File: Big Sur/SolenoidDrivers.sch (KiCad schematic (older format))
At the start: 35 parts, among them U1 DRV8806, U2 DRV8806, U3 DRV103H, U4 DRV103H

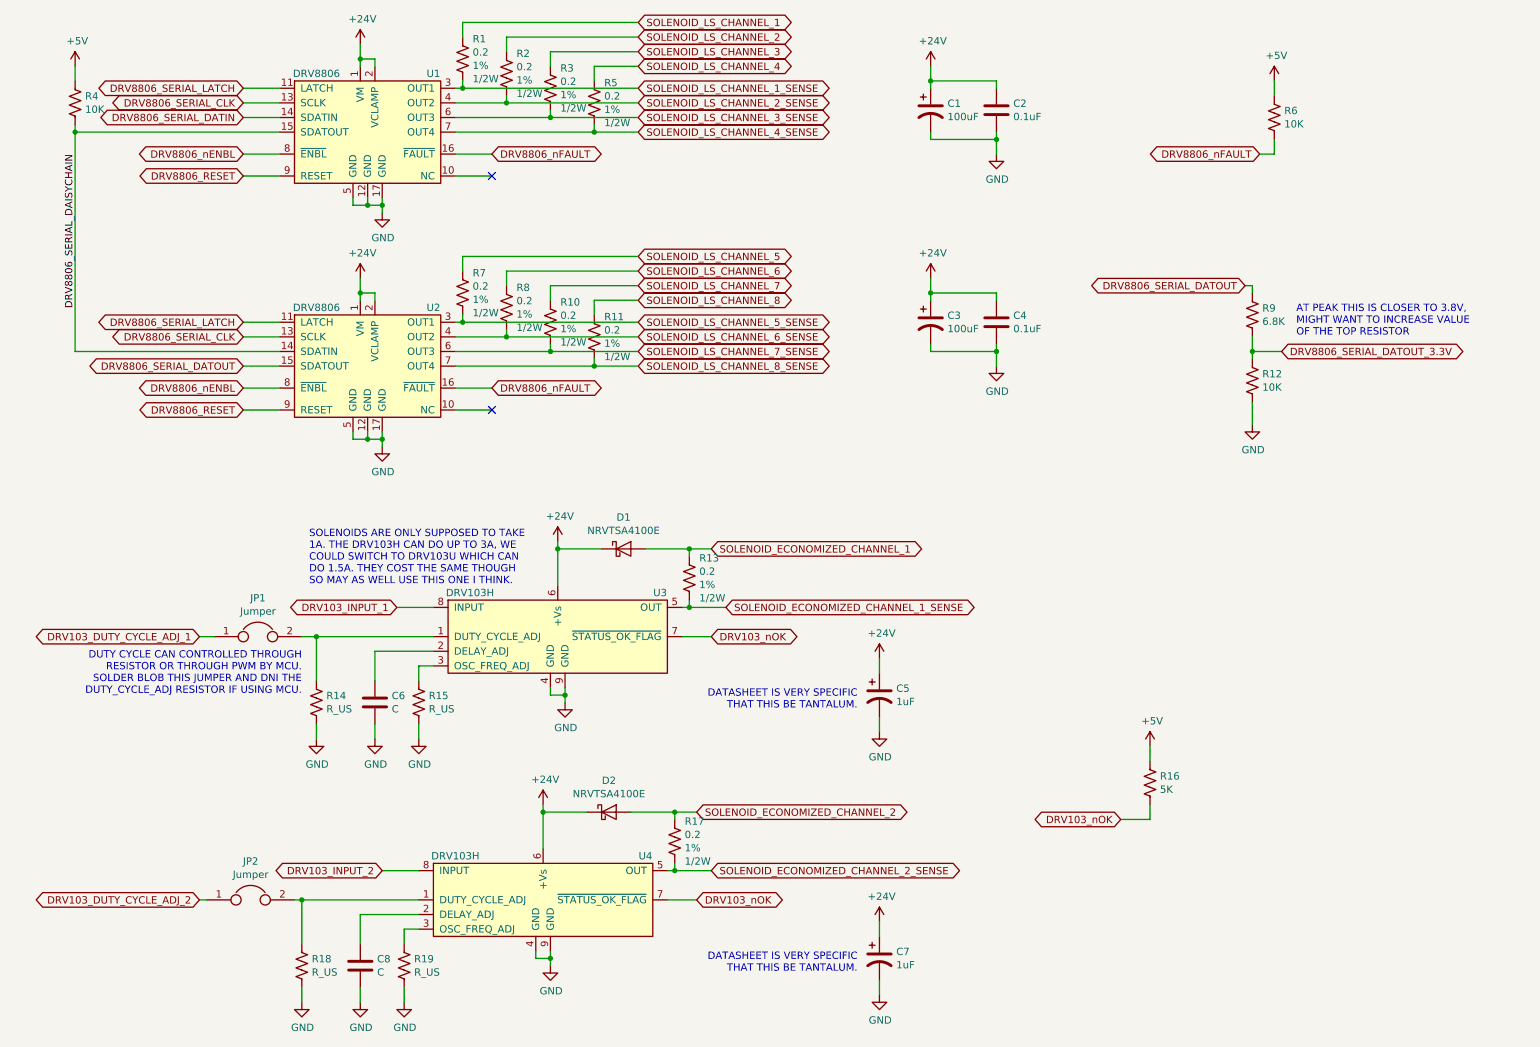
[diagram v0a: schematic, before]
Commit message: Updated current sense, second pump driver, solenoid connectors
-Current sense now uses current sense ICs, connected to Paraduino ADC pins.
-Added second pump driver.
-Connected outputs with XT30 connectors.
-Still need some Paraduino connections, inverter driver, footprints.
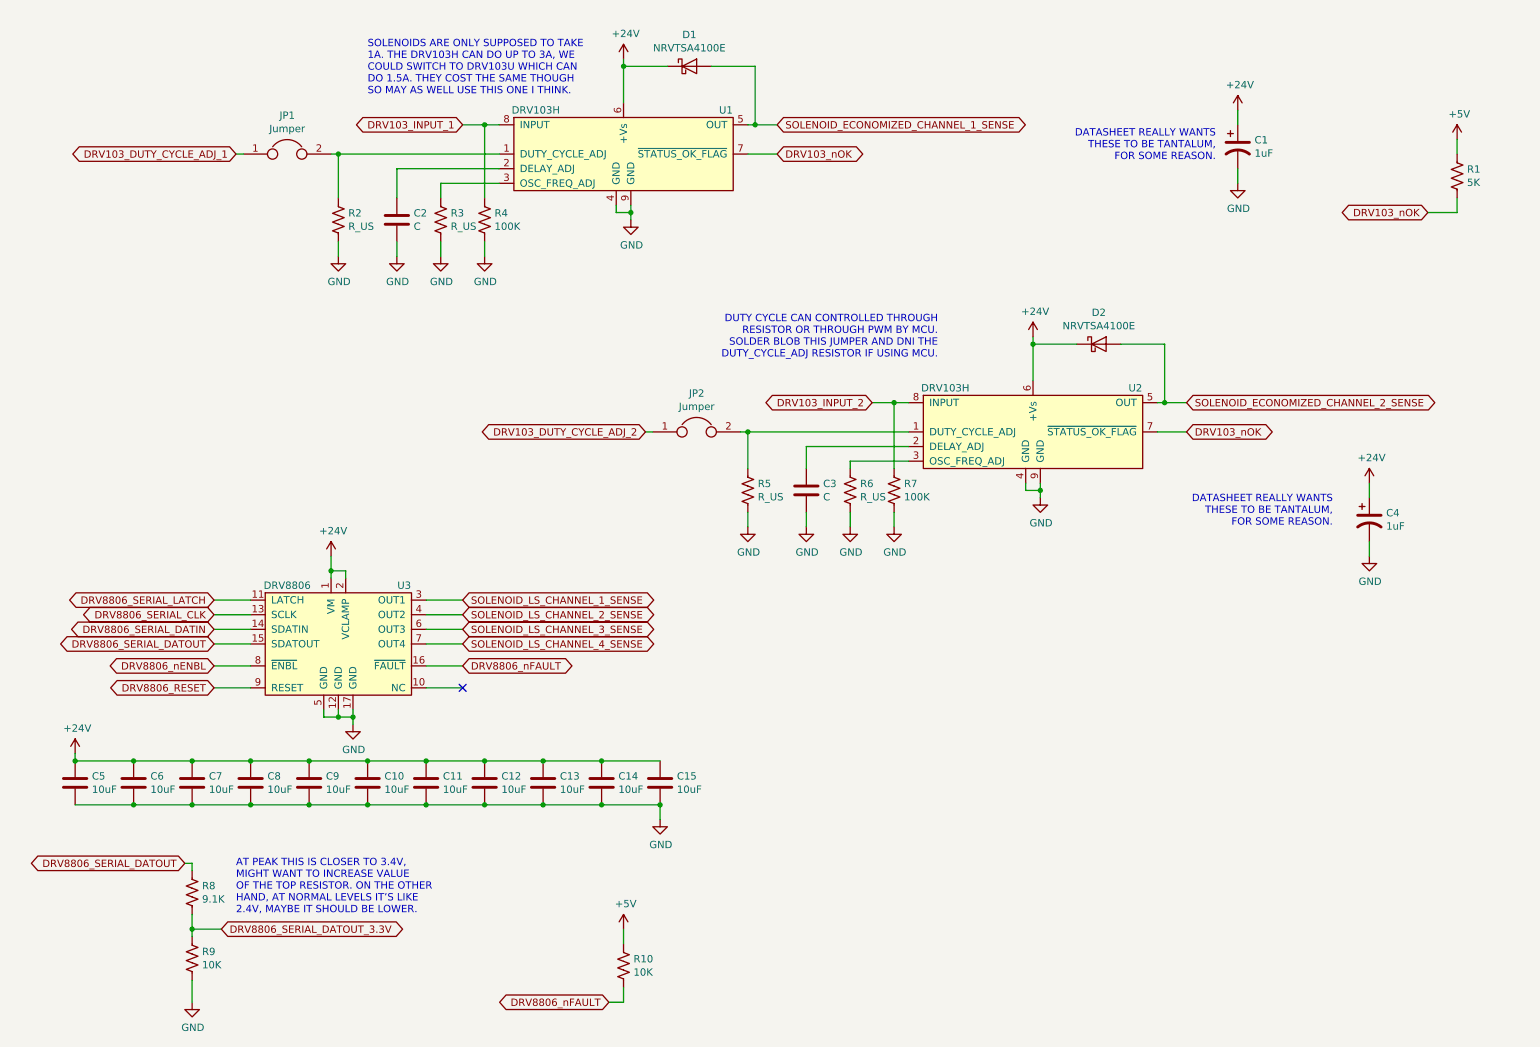
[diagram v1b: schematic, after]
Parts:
- removed C1, C3: 100uF, symbol Device:CP1
- removed C2, C4: 0.1uF, symbol Device:C
- removed C5: 1uF, symbol Device:CP1
- removed R1, R10, R11, R13, R17, R2, R3, R8: 0.2, symbol Device:R_US
- removed R18, R19: R_US, symbol Device:R_US
- removed U2: DRV8806, Package_SO:HTSSOP-16-1EP_4.4x5mm_P0.65mm_EP3.4x5mm_Mask2.46x2.31mm_ThermalVias, symbol BigSurLib:DRV8806
- added C10, C11, C12, C13, C14, C15, C5, C6, C7, C9: 10uF, Capacitor_SMD:C_1210_3225Metric_Pad1.42x2.65mm_HandSolder, symbol Device:C
- added C3: C, symbol Device:C
- added C4: 1uF, symbol Device:CP1
- added R6: R_US, symbol Device:R_US
- C1: renamed from C7; Digikey (none) -> https://www.digikey.ca/product-detail/en/kemet/T491C105K050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; Part Number (none) -> T491C105K050AT
- C8: value C -> 10uF; footprint (none) -> Capacitor_SMD:C_1210_3225Metric_Pad1.42x2.65mm_HandSolder; Digikey (none) -> https://www.digikey.ca/product-detail/en/taiyo-yuden/UMK325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; Part Number (none) -> UMK325BJ106KMHP
- R4: value 10K -> 100K
- R5: value 0.2 -> R_US; Power Rating 1/2W -> (none); Tolerance 1% -> (none)
- R7: value 0.2 -> 100K; Power Rating 1/2W -> (none); Tolerance 1% -> (none)
- R8: renamed from R9; value 6.8K -> 9.1K
- renumbered C6 to C2, R16 to R1, R6 to R10, R14 to R2, R15 to R3, R12 to R9, U3 to U1, U4 to U2, U1 to U3
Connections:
- net SOLENOID_ECONOMIZED_CHANNEL_1 is gone; now on net SOLENOID_ECONOMIZED_CHANNEL_1_SENSE: D1.2 (A)
- net SOLENOID_ECONOMIZED_CHANNEL_2 is gone; now on net SOLENOID_ECONOMIZED_CHANNEL_2_SENSE: D2.2 (A)
- net SOLENOID_LS_CHANNEL_4 is gone; now on net GND: R5.2
- net SOLENOID_LS_CHANNEL_5 is gone; now on net GND: R7.2
- net SOLENOID_LS_CHANNEL_5_SENSE is gone; now on net DRV103_INPUT_2: R7.1
- net +24V: now also C8.1, C10.1, C11.1, C12.1, C13.1, C14.1, C15.1, C4.1, C5.1, C6.1, C7.1, C9.1
- net +5V: no longer R4.1
- net DRV103_INPUT_1: now also R4.1
- net DRV8806_SERIAL_DATOUT: now also U3.15 (SDATOUT)
- net GND: now also R4.2, C10.2, C11.2, C12.2, C13.2, C14.2, C15.2, C3.2, C4.2, C5.2, C6.2, C7.2, C9.2, R6.2
- net SOLENOID_LS_CHANNEL_4_SENSE: no longer R5.1
- net at U2.3 (OSC_FREQ_ADJ): now also R6.1
- net at JP2.2, U2.1 (DUTY_CYCLE_ADJ): now also R5.1
- net at U2.2 (DELAY_ADJ): now also C3.1; no longer C8.1
- removed net DRV8806_SERIAL_DAISYCHAIN: R4.2, U3.15 (SDATOUT)
- no-connect marks 2 -> 1
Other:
- note added: "AT PEAK THIS IS CLOSER TO 3.4V,\nMIGHT WANT TO INCREASE VALUE\nOF THE TOP RESISTOR. ON THE OTHER\nHAND, AT NORMAL LEVELS IT’S LIKE\n2.4V, MAYBE IT SHOULD BE LOWER."
- note added: "DATASHEET REALLY WANTS\nTHESE TO BE TANTALUM,\nFOR SOME REASON."
- note removed: "AT PEAK THIS IS CLOSER TO 3.8V,\nMIGHT WANT TO INCREASE VALUE\nOF THE TOP RESISTOR"
- note removed: "DATASHEET IS VERY SPECIFIC\nTHAT THIS BE TANTALUM."
- moved on the sheet: C1, C2, D1, D2, JP1, R1, R10, R2, R3, R8, R9, U1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

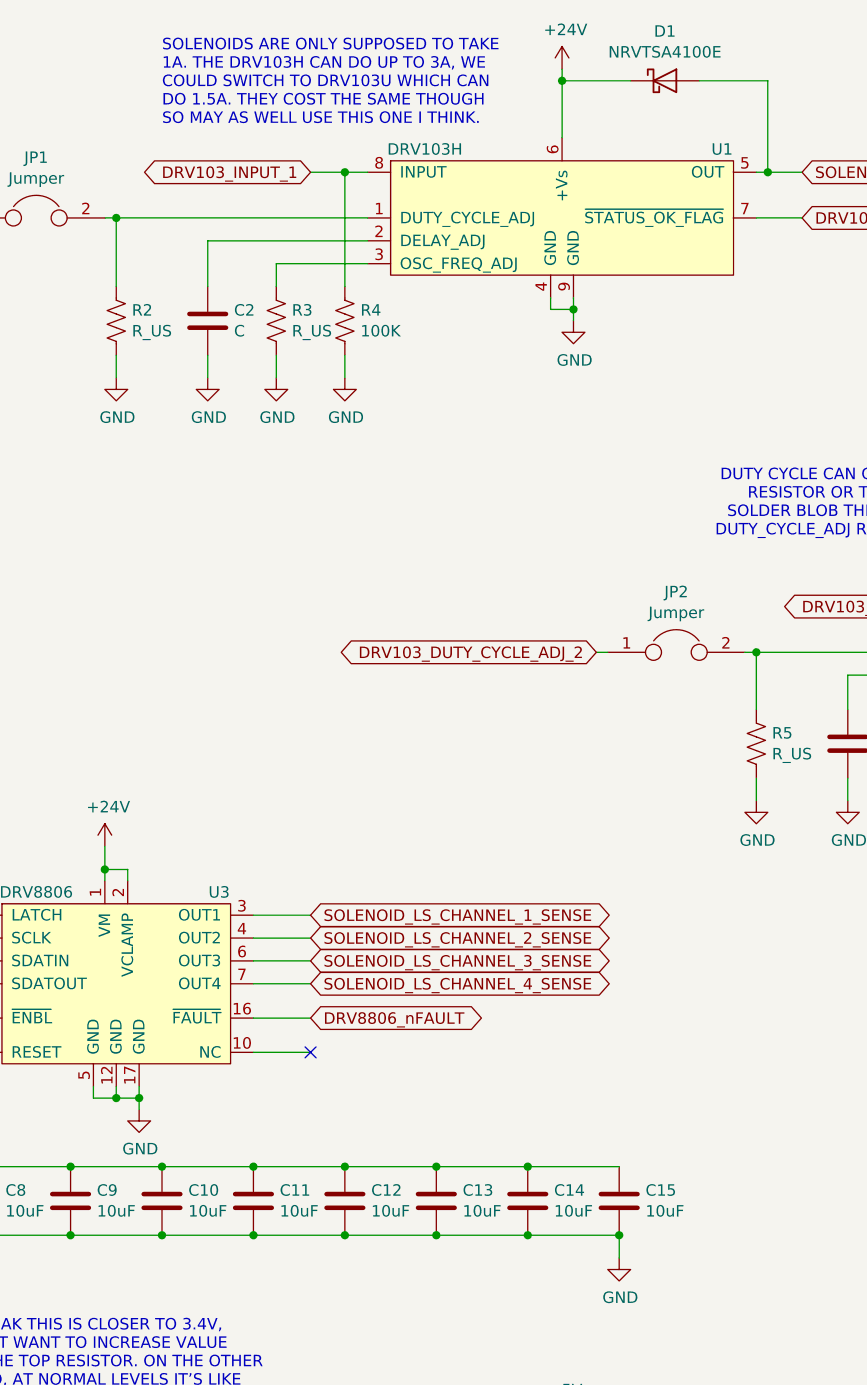
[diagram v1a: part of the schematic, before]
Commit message: Removed Inverter
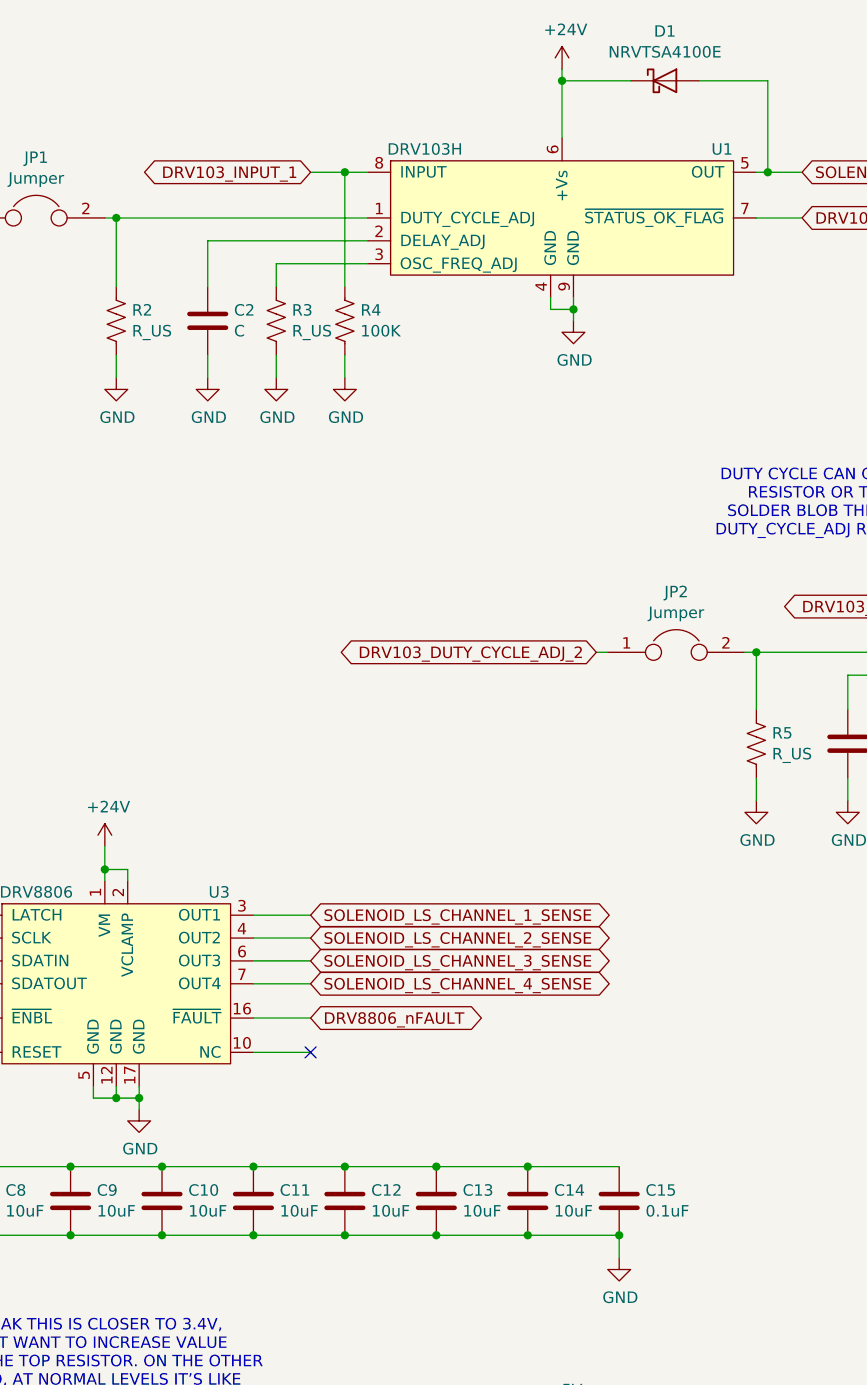
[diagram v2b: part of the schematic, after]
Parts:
- C15: value 10uF -> 0.1uF; footprint Capacitor_SMD:C_1210_3225Metric_Pad1.42x2.65mm_HandSolder -> Capacitor_SMD:C_0603_1608Metric_Pad1.05x0.95mm_HandSolder; Digikey https://www.digikey.ca/product-detail/en/taiyo-yuden/UMK325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 -> https://www.digikey.ca/product-detail/en/samsung-electro-me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; Part Number UMK325BJ106KMHP -> CL10B104KB8NNNC
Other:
- note removed: "SOLENOIDS ARE ONLY SUPPOSED TO TAKE\n1A. THE DRV103H CAN DO UP TO 3A, WE\nCOULD SWITCH TO DRV103U WHICH CAN\nDO 1.5A. THEY COST THE SAME THOUGH\nSO MAY AS WELL USE THIS ONE I THINK."
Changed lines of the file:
@@
 Comp "Paradigm Hyperloop"
 Comment1 ""
-Comment2 ""
-Comment3 ""
+Comment2 "x"
+Comment3 "x"
 Comment4 "Jasper Rubin"
 $EndDescr
@@
 Text Notes 6800 3100 2    50   ~ 0
 DUTY CYCLE CAN CONTROLLED THROUGH\nRESISTOR OR THROUGH PWM BY MCU.\nSOLDER BLOB THIS JUMPER AND DNI THE\nDUTY_CYCLE_ADJ RESISTOR IF USING MCU.
-Text Notes 2900 1300 0    50   ~ 0
-SOLENOIDS ARE ONLY SUPPOSED TO TAKE\n1A. THE DRV103H CAN DO UP TO 3A, WE\nCOULD SWITCH TO DRV103U WHICH CAN\nDO 1.5A. THEY COST THE SAME THOUGH\nSO MAY AS WELL USE THIS ONE I THINK.
 Text GLabel 3550 1500 0    50   BiDi ~ 0
 DRV103_INPUT_1
@@
 AR Path="/5D765C4F/5DF36911" Ref="C?"  Part="1"
 F 0 "C15" H 5015 6046 50  0000 L CNN
-F 1 "10uF" H 5015 5955 50  0000 L CNN
-F 2 "Capacitor_SMD:C_1210_3225Metric_Pad1.42x2.65mm_HandSolder" H 4900 6000 50  0001 C CNN
-F 3 "https://ds.yuden.co.jp/TYCOMPAS/ut/detail?pn=UMK325BJ106KMHP%20&u=M" H 4900 6000 50  0001 C CNN
-F 4 "UMK325BJ106KMHP" H 4900 6000 50  0001 C CNN "Part Number"
-F 5 "https://www.digikey.ca/product-detail/en/taiyo-yuden/UMK325BJ106KMHP/587-5961-1-ND/7675081" H 4900 6000 50  0001 C CNN "Digikey"
+F 1 "0.1uF" H 5015 5955 50  0000 L CNN
+F 2 "Capacitor_SMD:C_0603_1608Metric_Pad1.05x0.95mm_HandSolder" H 4900 6000 50  0001 C CNN
+F 3 "http://www.samsungsem.com/kr/support/product-search/mlcc/__icsFiles/afieldfile/2019/06/18/CL10B104KB8NNNC-19.pdf" H 4900 6000 50  0001 C CNN
+F 4 "CL10B104KB8NNNC" H 4900 6000 50  0001 C CNN "Part Number"
+F 5 "https://www.digikey.ca/product-detail/en/samsung-electro-mechanics/CL10B104KB8NNNC/1276-1000-1-ND/3889086" H 4900 6000 50  0001 C CNN "Digikey"
 	1    4900 6000
 	1    0    0    -1
